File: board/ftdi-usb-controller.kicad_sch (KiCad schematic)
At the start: 25 parts, among them U1 93LC46B, U2 FT2232HQ, Y1 12MHz

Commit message: Complete schematic
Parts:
- renumbered C29 to C23, C30 to C24, C31 to C25, C32 to C26, C33 to C27, C34 to C28, C35 to C29, C36 to C30, C37 to C31, C38 to C32, C39 to C33, C40 to C34, C41 to C35, C42 to C36
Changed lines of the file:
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@@
 		(dnp no)
 		(fields_autoplaced yes)
-		(property "Reference" "C39"
+		(property "Reference" "C33"
 			(at 104.14 85.0899 0)
 			(effects
@@
 			(project "HispalisFPGA"
 				(path "/864346d0-d3ef-428e-a44f-9476f195db98/b100cd7e-168e-400b-b229-504b7bfa854d"
-					(reference "C39")
+					(reference "C33")
 					(unit 1)
 				)
@@
 		(dnp no)
 		(fields_autoplaced yes)
-		(property "Reference" "C31"
+		(property "Reference" "C25"
 			(at 62.23 85.0899 0)
 			(effects
@@
 			(project "HispalisFPGA"
 				(path "/864346d0-d3ef-428e-a44f-9476f195db98/b100cd7e-168e-400b-b229-504b7bfa854d"
-					(reference "C31")
+					(reference "C25")
 					(unit 1)
 				)
@@
 		(dnp no)
 		(fields_autoplaced yes)
-		(property "Reference" "C29"
+		(property "Reference" "C23"
 			(at 39.37 189.2299 0)
 			(effects
@@
 			(project "HispalisFPGA"
 				(path "/864346d0-d3ef-428e-a44f-9476f195db98/b100cd7e-168e-400b-b229-504b7bfa854d"
-					(reference "C29")
+					(reference "C23")
 					(unit 1)
 				)
@@
 		(dnp no)
 		(fields_autoplaced yes)
-		(property "Reference" "C37"
+		(property "Reference" "C31"
 			(at 90.17 85.0899 0)
 			(effects
@@
 			(project "HispalisFPGA"
 				(path "/864346d0-d3ef-428e-a44f-9476f195db98/b100cd7e-168e-400b-b229-504b7bfa854d"
-					(reference "C37")
+					(reference "C31")
 					(unit 1)
 				)
@@
 		(on_board yes)
 		(dnp no)
-		(property "Reference" "C34"
+		(property "Reference" "C28"
 			(at 77.47 186.944 90)
 			(effects
@@
 			(project "HispalisFPGA"
 				(path "/864346d0-d3ef-428e-a44f-9476f195db98/b100cd7e-168e-400b-b229-504b7bfa854d"
-					(reference "C34")
+					(reference "C28")
 					(unit 1)
 				)
@@
 		(dnp no)
 		(fields_autoplaced yes)
-		(property "Reference" "C32"
+		(property "Reference" "C26"
 			(at 68.58 111.7599 0)
 			(effects
@@
 			(project "HispalisFPGA"
 				(path "/864346d0-d3ef-428e-a44f-9476f195db98/b100cd7e-168e-400b-b229-504b7bfa854d"
-					(reference "C32")
+					(reference "C26")
 					(unit 1)
 				)
@@
 		(dnp no)
 		(fields_autoplaced yes)
-		(property "Reference" "C30"
+		(property "Reference" "C24"
 			(at 54.61 111.7599 0)
 			(effects
@@
 			(project "HispalisFPGA"
 				(path "/864346d0-d3ef-428e-a44f-9476f195db98/b100cd7e-168e-400b-b229-504b7bfa854d"
-					(reference "C30")
+					(reference "C24")
 					(unit 1)
 				)
@@
 		(on_board yes)
 		(dnp no)
-		(property "Reference" "C41"
+		(property "Reference" "C35"
 			(at 158.75 73.6599 0)
 			(effects
@@
 			(project "HispalisFPGA"
 				(path "/864346d0-d3ef-428e-a44f-9476f195db98/b100cd7e-168e-400b-b229-504b7bfa854d"
-					(reference "C41")
+					(reference "C35")
 					(unit 1)
 				)
@@
 		(on_board yes)
 		(dnp no)
-		(property "Reference" "C35"
+		(property "Reference" "C29"
 			(at 77.47 206.756 90)
 			(effects
@@
 			(project "HispalisFPGA"
 				(path "/864346d0-d3ef-428e-a44f-9476f195db98/b100cd7e-168e-400b-b229-504b7bfa854d"
-					(reference "C35")
+					(reference "C29")
 					(unit 1)
 				)
@@
 		(on_board yes)
 		(dnp no)
-		(property "Reference" "C42"
+		(property "Reference" "C36"
 			(at 172.72 73.6599 0)
 			(effects
@@
 			(project "HispalisFPGA"
 				(path "/864346d0-d3ef-428e-a44f-9476f195db98/b100cd7e-168e-400b-b229-504b7bfa854d"
-					(reference "C42")
+					(reference "C36")
 					(unit 1)
 				)
@@
 		(dnp no)
 		(fields_autoplaced yes)
-		(property "Reference" "C36"
+		(property "Reference" "C30"
 			(at 82.55 111.7599 0)
 			(effects
@@
 			(project "HispalisFPGA"
 				(path "/864346d0-d3ef-428e-a44f-9476f195db98/b100cd7e-168e-400b-b229-504b7bfa854d"
-					(reference "C36")
+					(reference "C30")
 					(unit 1)
 				)
@@
 		(on_board yes)
 		(dnp no)
-		(property "Reference" "C38"
+		(property "Reference" "C32"
 			(at 86.36 119.3799 0)
 			(effects
@@
 			(project "HispalisFPGA"
 				(path "/864346d0-d3ef-428e-a44f-9476f195db98/b100cd7e-168e-400b-b229-504b7bfa854d"
-					(reference "C38")
+					(reference "C32")
 					(unit 1)
 				)
@@
 		(dnp no)
 		(fields_autoplaced yes)
-		(property "Reference" "C33"
+		(property "Reference" "C27"
 			(at 76.2 85.0899 0)
 			(effects
@@
 			(project "HispalisFPGA"
 				(path "/864346d0-d3ef-428e-a44f-9476f195db98/b100cd7e-168e-400b-b229-504b7bfa854d"
-					(reference "C33")
+					(reference "C27")
 					(unit 1)
 				)
@@
 		(on_board yes)
 		(dnp no)
-		(property "Reference" "C40"
+		(property "Reference" "C34"
 			(at 144.78 73.6599 0)
 			(effects
@@
 			(project "HispalisFPGA"
 				(path "/864346d0-d3ef-428e-a44f-9476f195db98/b100cd7e-168e-400b-b229-504b7bfa854d"
-					(reference "C40")
-					(unit 1)
-				)
+					(reference "C34")
+					(unit 1)
+				)

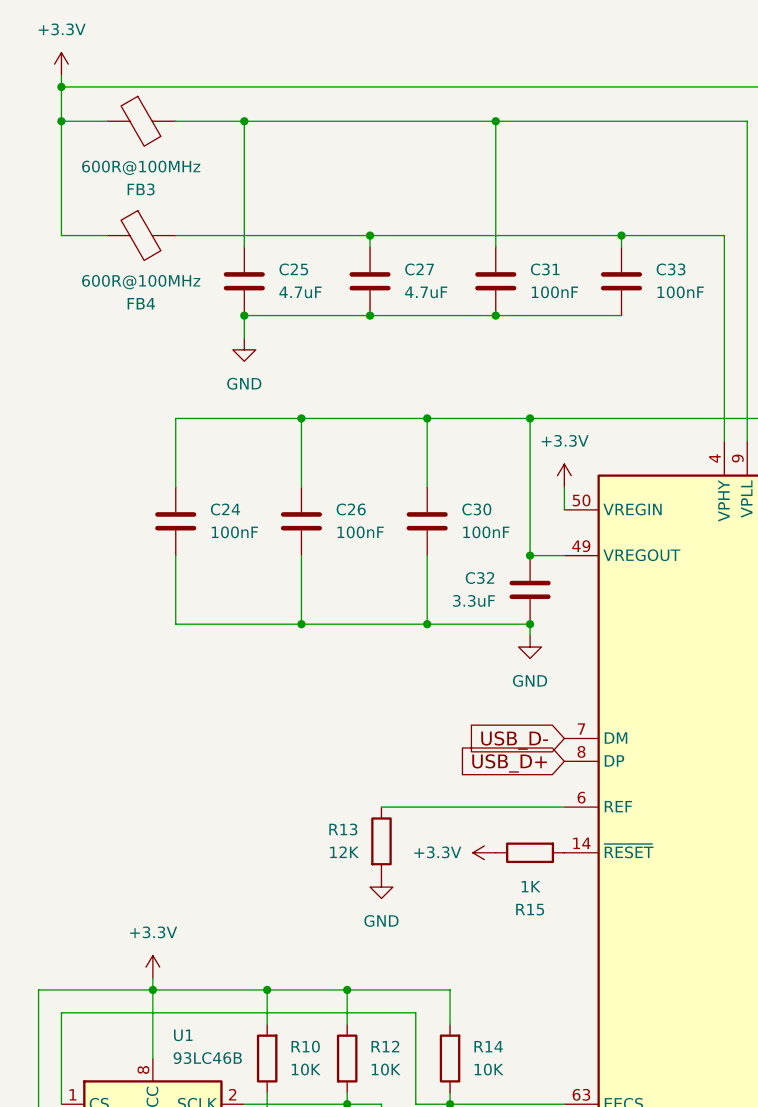
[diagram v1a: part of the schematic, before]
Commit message: Finish routing and remove unneeded silkscreen
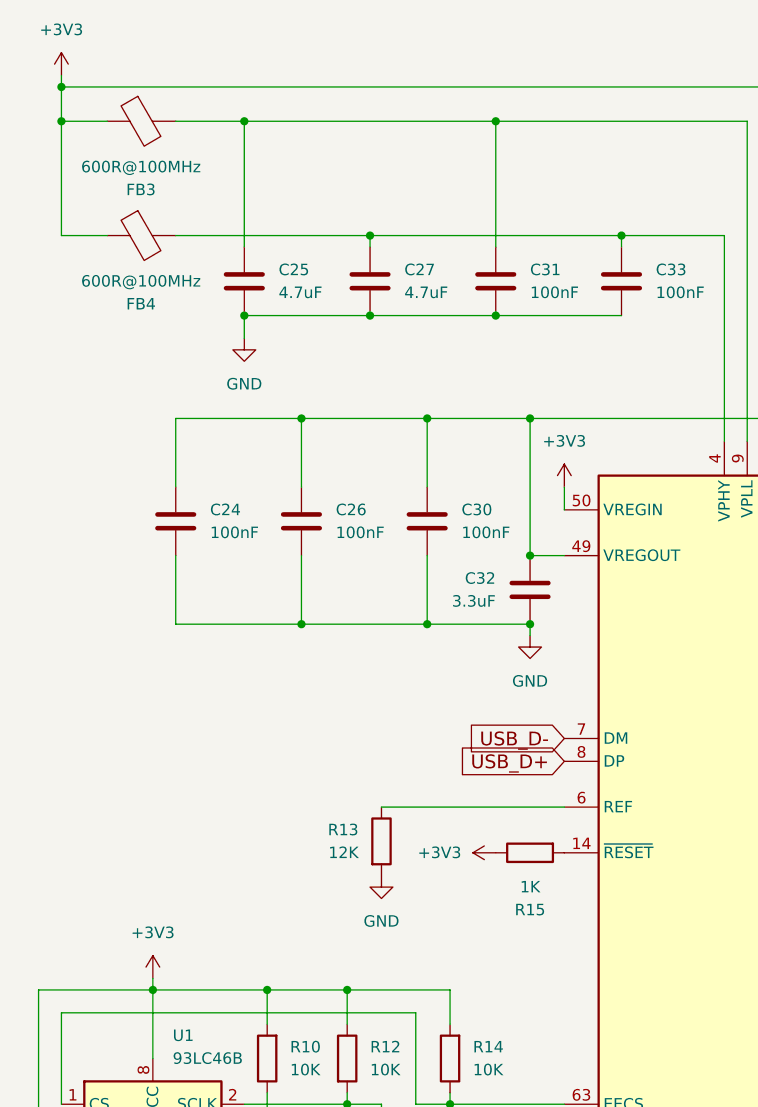
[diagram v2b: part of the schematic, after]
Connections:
- net +3.3V renamed +3V3

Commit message: Add metadata
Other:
- company: (none) -> Alejandro Domínguez Muñoz
- title: (none) -> HispalisFPGA USB Controller for JTAG and UART
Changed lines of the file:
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@@
 	(generator_version "8.0")
 	(paper "A4" portrait)
+	(title_block
+		(title "HispalisFPGA USB Controller for JTAG and UART")
+		(date "2024-10-21")
+		(rev "A")
+		(company "Alejandro Domínguez Muñoz")
+	)
 	(junction
 		(at 85.09 200.66)
